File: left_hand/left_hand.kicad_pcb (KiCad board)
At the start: 2 copper layers, 75 x 85 mm, 48 parts, among them J1 8P8C_Shielded, J2 Conn_01x08, J3 Conn_01x03, J4 Conn_01x08, J5 Conn_02x02_Top_Bottom, J6 Screw_Terminal_01x10, M1 Motor_Servo, M2 Motor_Servo, M3 Motor_Servo, M4 Motor_Servo, M5 Motor_Servo, Q1 Q_NMOS_GDS, Q2 Q_NMOS_GDS, Q3 Q_NMOS_GDS, Q4 Q_NMOS_GDS, Q5 Q_NMOS_GDS, U1 MCP23017_SP, U2 PCA9615DP, U3 PCA9685PW

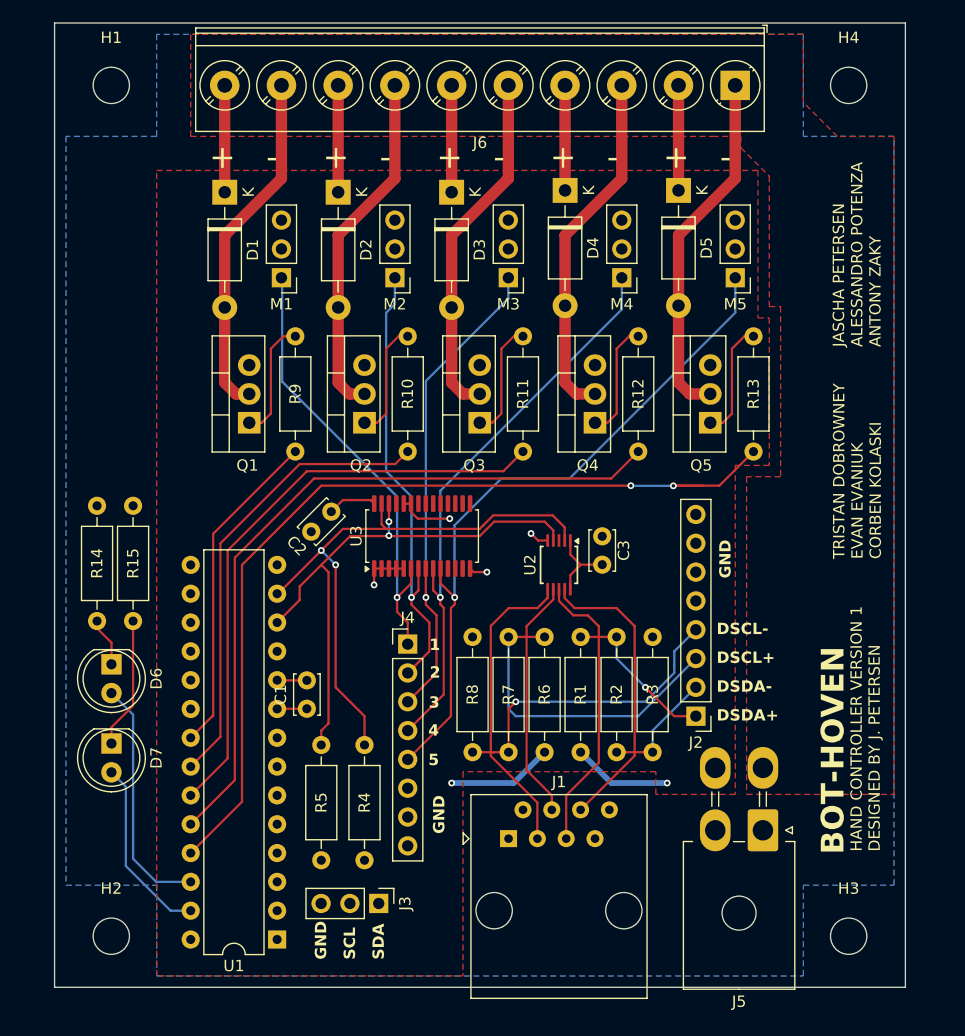
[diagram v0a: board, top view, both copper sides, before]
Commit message: Added current and voltage sensing on control board
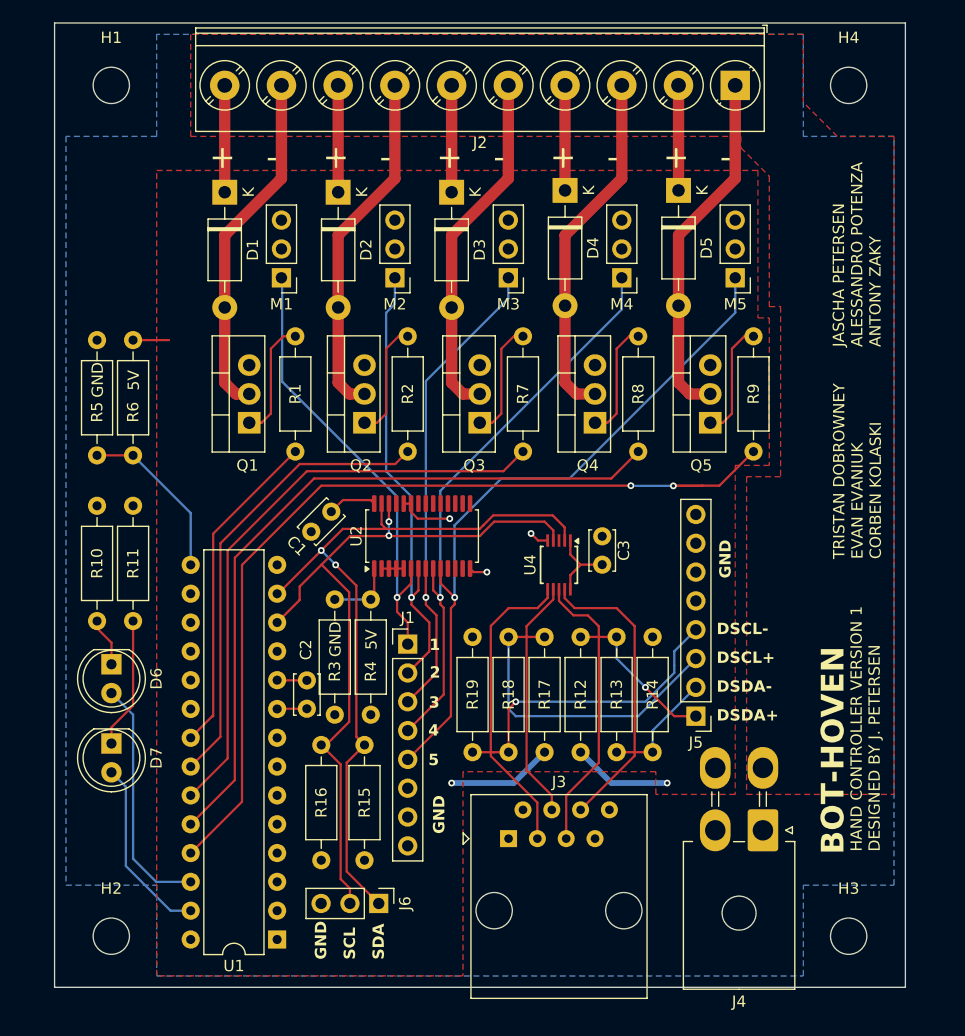
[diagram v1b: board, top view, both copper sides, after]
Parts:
- added R3: 0R, Resistor_THT:R_Axial_DIN0207_L6.3mm_D2.5mm_P10.16mm_Horizontal, F.Cu at (139.7, 107.3)
- added R4: 0R, Resistor_THT:R_Axial_DIN0207_L6.3mm_D2.5mm_P10.16mm_Horizontal, F.Cu at (142.9, 107.3)
- added R5: 0R, Resistor_THT:R_Axial_DIN0207_L6.3mm_D2.5mm_P10.16mm_Horizontal, F.Cu at (118.7, 94.6)
- added R6: 0R, Resistor_THT:R_Axial_DIN0207_L6.3mm_D2.5mm_P10.16mm_Horizontal, F.Cu at (121.9, 94.6)
- renumbered C2 to C1, C1 to C2, J4 to J1, J6 to J2, J1 to J3, J5 to J4, J2 to J5, J3 to J6, R9 to R1, R14 to R10, R15 to R11, R1 to R12, R2 to R13, R3 to R14, R4 to R15, R5 to R16, R6 to R17, R7 to R18, R8 to R19, R10 to R2, R11 to R7, R12 to R8, R13 to R9, U3 to U2, U2 to U4
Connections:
- U1 pad 15: GND -> Net-(U1-A0)
- U2 pad 1: GND -> Net-(U2-A0)
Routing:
- net SCL: track 49.2 -> 66.0 mm
- net SDA: track 51.0 -> 66.8 mm
- net Net-(U1-A0): track 0.00 -> 14.9 mm
- net Net-(U2-A0): track 0.00 -> 6.02 mm
- net +5V: track 31.7 -> 34.9 mm
- net GND: track 15.1 -> 13.0 mm, vias 4 -> 3
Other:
- board text added: "5V"

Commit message: Added limit switches to hand and readme
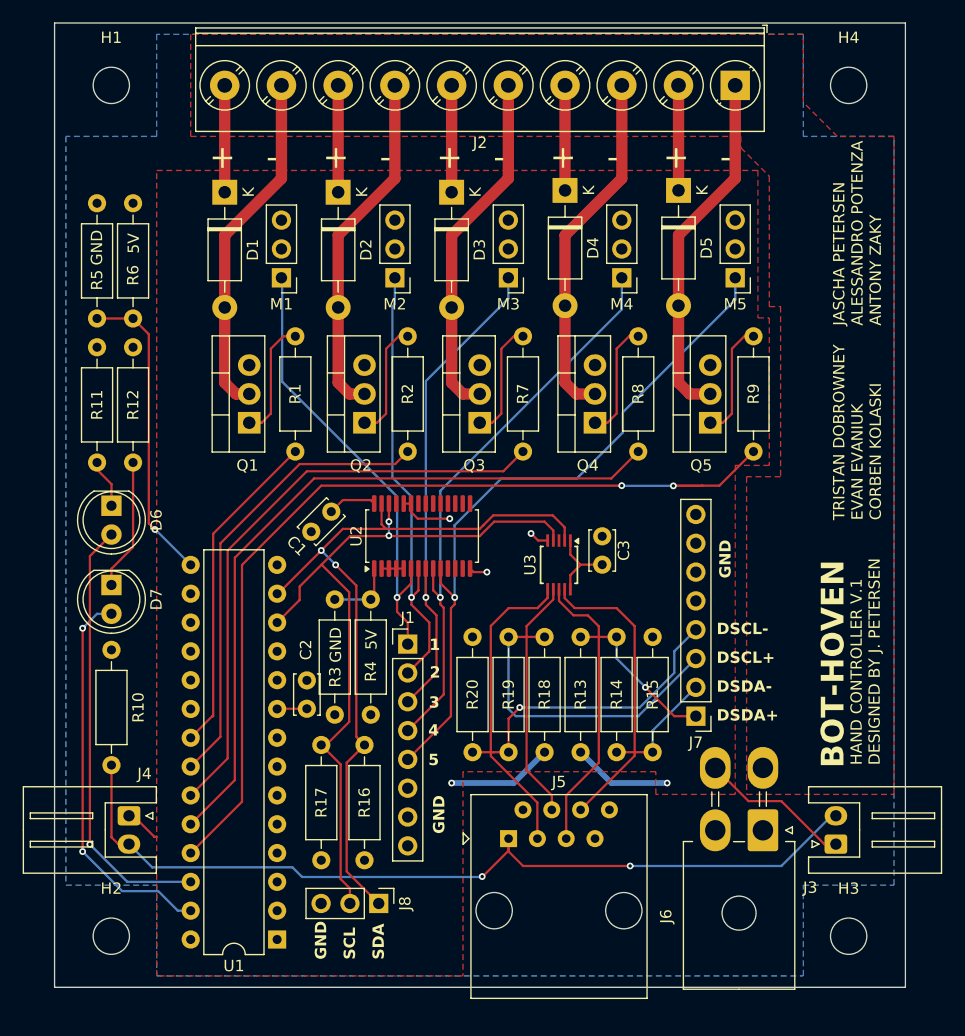
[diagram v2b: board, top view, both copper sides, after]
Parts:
- added J3: Conn_01x02, Connector_JST:JST_XH_S2B-XH-A_1x02_P2.50mm_Horizontal, F.Cu at (183.9, 128.9)
- added J4: Conn_01x02, Connector_JST:JST_XH_S2B-XH-A_1x02_P2.50mm_Horizontal, F.Cu at (121.6, 126.4)
- added R10: 10k, Resistor_THT:R_Axial_DIN0207_L6.3mm_D2.5mm_P10.16mm_Horizontal, F.Cu at (120.0, 111.8)
- moved D6 14.0 mm to (120.0, 99.1)
- moved D7 14.0 mm to (120.0, 106.0)
- moved R11 14.0 mm to (118.7, 95.2)
- moved R12 14.0 mm to (121.9, 95.2)
- moved R5 12.1 mm to (118.7, 82.5)
- moved R6 12.1 mm to (121.9, 82.5)
- renumbered J3 to J5, J4 to J6, J5 to J7, J6 to J8, R10 to R11, R11 to R12, R12 to R13, R13 to R14, R14 to R15, R15 to R16, R16 to R17, R17 to R18, R18 to R19, R19 to R20, U4 to U3
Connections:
- J5 pad 1: GND -> LIMIT_SW
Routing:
- net LIMIT_SW: track 0.00 -> 77.2 mm, vias 0 -> 2
- net LED2: track 16.1 -> 34.4 mm, vias 0 -> 2
- net LED1: track 21.3 -> 38.4 mm, vias 0 -> 1
- net +5V: track 34.9 -> 48.4 mm
- net Net-(U1-A0): track 14.9 -> 27.0 mm, vias 0 -> 1
- net GND: track 13.0 -> 10.4 mm
- net DSCL-: track 55.0 -> 54.5 mm
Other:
- board text added: "HAND CONTROLLER V.1"
- board text removed: "HAND CONTROLLER VERSION 1"

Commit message: Started layout of control board
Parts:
- added R21: 10k, Resistor_THT:R_Axial_DIN0207_L6.3mm_D2.5mm_P10.16mm_Horizontal, F.Cu at (180.3, 108.0)
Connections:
- J3 pad 2: LIMIT_SW -> LIMIT_SW_R
- J4 pad 2: LIMIT_SW -> LIMIT_SW_L
- J5 pad 1: LIMIT_SW -> LIMIT_SW_L
- J5 pad 8: GND -> LIMIT_SW_R
- R10 pad 2: LIMIT_SW -> LIMIT_SW_L
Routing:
- net LIMIT_SW: track 77.2 -> 0.00 mm, vias 2 -> 0
- net LIMIT_SW_L: track 0.00 -> 44.9 mm, vias 0 -> 1
- net LIMIT_SW_R: track 0.00 -> 34.2 mm, vias 0 -> 2

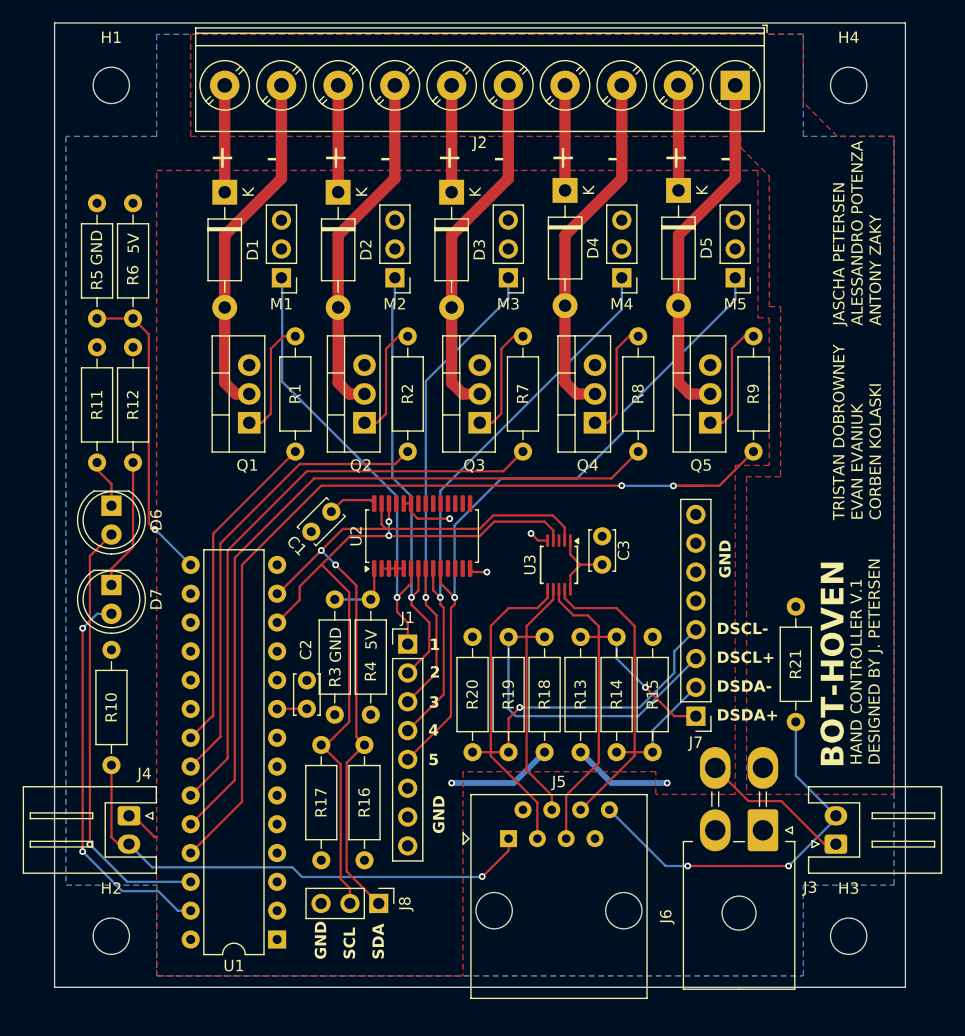
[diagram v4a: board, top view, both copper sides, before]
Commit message: Completed control board layout
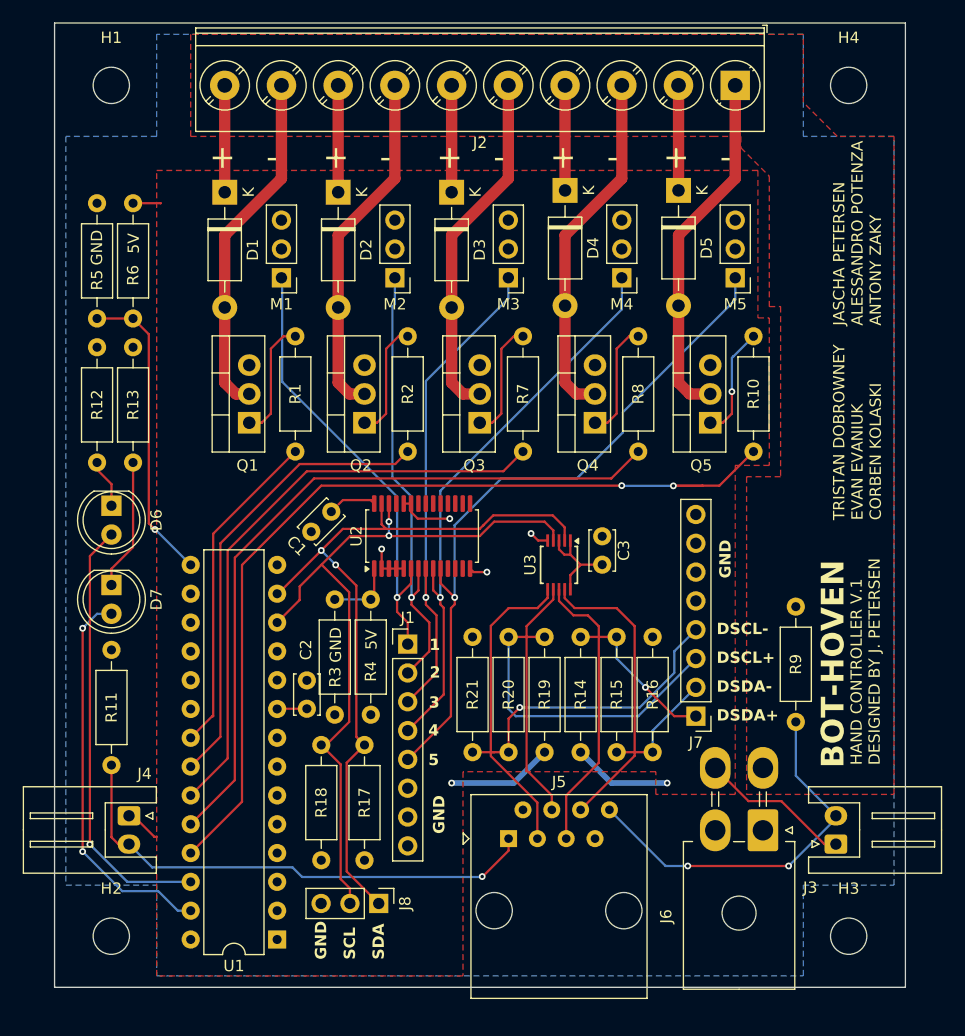
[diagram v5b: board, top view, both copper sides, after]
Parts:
- renumbered R9 to R10, R10 to R11, R11 to R12, R12 to R13, R13 to R14, R14 to R15, R15 to R16, R16 to R17, R17 to R18, R18 to R19, R19 to R20, R20 to R21, R21 to R9
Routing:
- net +5V: track 48.4 -> 52.8 mm
- net GND: track 10.4 -> 12.1 mm, vias 3 -> 4
- net Net-(Q5-G): track 10.3 -> 9.84 mm, vias 0 -> 1
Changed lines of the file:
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@@
 		(descr "Resistor, Axial_DIN0207 series, Axial, Horizontal, pin pitch=10.16mm, 0.25W = 1/4W, length*diameter=6.3*2.5mm^2, http://cdn-reichelt.de/documents/datenblatt/B400/1_4W%23YAG.pdf")
 		(tags "Resistor Axial_DIN0207 series Axial Horizontal pin pitch 10.16mm 0.25W = 1/4W length 6.3mm diameter 2.5mm")
-		(property "Reference" "R20"
+		(property "Reference" "R21"
 			(at 5.08 0 90)
 			(layer "F.SilkS")
@@
 		(descr "Resistor, Axial_DIN0207 series, Axial, Horizontal, pin pitch=10.16mm, 0.25W = 1/4W, length*diameter=6.3*2.5mm^2, http://cdn-reichelt.de/documents/datenblatt/B400/1_4W%23YAG.pdf")
 		(tags "Resistor Axial_DIN0207 series Axial Horizontal pin pitch 10.16mm 0.25W = 1/4W length 6.3mm diameter 2.5mm")
-		(property "Reference" "R15"
+		(property "Reference" "R16"
 			(at 5.08 0 90)
 			(layer "F.SilkS")
@@
 		(descr "Resistor, Axial_DIN0207 series, Axial, Horizontal, pin pitch=10.16mm, 0.25W = 1/4W, length*diameter=6.3*2.5mm^2, http://cdn-reichelt.de/documents/datenblatt/B400/1_4W%23YAG.pdf")
 		(tags "Resistor Axial_DIN0207 series Axial Horizontal pin pitch 10.16mm 0.25W = 1/4W length 6.3mm diameter 2.5mm")
-		(property "Reference" "R12"
+		(property "Reference" "R13"
 			(at 5.08 0 90)
 			(layer "F.SilkS")
@@
 		(descr "Resistor, Axial_DIN0207 series, Axial, Horizontal, pin pitch=10.16mm, 0.25W = 1/4W, length*diameter=6.3*2.5mm^2, http://cdn-reichelt.de/documents/datenblatt/B400/1_4W%23YAG.pdf")
 		(tags "Resistor Axial_DIN0207 series Axial Horizontal pin pitch 10.16mm 0.25W = 1/4W length 6.3mm diameter 2.5mm")
-		(property "Reference" "R11"
+		(property "Reference" "R12"
 			(at 5.08 0 90)
 			(layer "F.SilkS")
@@
 		(descr "Resistor, Axial_DIN0207 series, Axial, Horizontal, pin pitch=10.16mm, 0.25W = 1/4W, length*diameter=6.3*2.5mm^2, http://cdn-reichelt.de/documents/datenblatt/B400/1_4W%23YAG.pdf")
 		(tags "Resistor Axial_DIN0207 series Axial Horizontal pin pitch 10.16mm 0.25W = 1/4W length 6.3mm diameter 2.5mm")
-		(property "Reference" "R9"
+		(property "Reference" "R10"
 			(at 5.08 0 90)
 			(layer "F.SilkS")
@@
 		(descr "Resistor, Axial_DIN0207 series, Axial, Horizontal, pin pitch=10.16mm, 0.25W = 1/4W, length*diameter=6.3*2.5mm^2, http://cdn-reichelt.de/documents/datenblatt/B400/1_4W%23YAG.pdf")
 		(tags "Resistor Axial_DIN0207 series Axial Horizontal pin pitch 10.16mm 0.25W = 1/4W length 6.3mm diameter 2.5mm")
-		(property "Reference" "R17"
+		(property "Reference" "R18"
 			(at 5.08 0 90)
 			(layer "F.SilkS")
@@
 		(descr "Resistor, Axial_DIN0207 series, Axial, Horizontal, pin pitch=10.16mm, 0.25W = 1/4W, length*diameter=6.3*2.5mm^2, http://cdn-reichelt.de/documents/datenblatt/B400/1_4W%23YAG.pdf")
 		(tags "Resistor Axial_DIN0207 series Axial Horizontal pin pitch 10.16mm 0.25W = 1/4W length 6.3mm diameter 2.5mm")
-		(property "Reference" "R14"
+		(property "Reference" "R15"
 			(at 5.08 0 90)
 			(layer "F.SilkS")
@@
 		(descr "Resistor, Axial_DIN0207 series, Axial, Horizontal, pin pitch=10.16mm, 0.25W = 1/4W, length*diameter=6.3*2.5mm^2, http://cdn-reichelt.de/documents/datenblatt/B400/1_4W%23YAG.pdf")
 		(tags "Resistor Axial_DIN0207 series Axial Horizontal pin pitch 10.16mm 0.25W = 1/4W length 6.3mm diameter 2.5mm")
-		(property "Reference" "R10"
+		(property "Reference" "R11"
 			(at 5.08 0 90)
 			(layer "F.SilkS")
@@
 		(descr "Resistor, Axial_DIN0207 series, Axial, Horizontal, pin pitch=10.16mm, 0.25W = 1/4W, length*diameter=6.3*2.5mm^2, http://cdn-reichelt.de/documents/datenblatt/B400/1_4W%23YAG.pdf")
 		(tags "Resistor Axial_DIN0207 series Axial Horizontal pin pitch 10.16mm 0.25W = 1/4W length 6.3mm diameter 2.5mm")
-		(property "Reference" "R18"
+		(property "Reference" "R19"
 			(at 5.08 0 90)
 			(layer "F.SilkS")
@@
 		(descr "Resistor, Axial_DIN0207 series, Axial, Horizontal, pin pitch=10.16mm, 0.25W = 1/4W, length*diameter=6.3*2.5mm^2, http://cdn-reichelt.de/documents/datenblatt/B400/1_4W%23YAG.pdf")
 		(tags "Resistor Axial_DIN0207 series Axial Horizontal pin pitch 10.16mm 0.25W = 1/4W length 6.3mm diameter 2.5mm")
-		(property "Reference" "R19"
+		(property "Reference" "R20"
 			(at 5.08 0 90)
 			(layer "F.SilkS")
@@
 		(descr "Resistor, Axial_DIN0207 series, Axial, Horizontal, pin pitch=10.16mm, 0.25W = 1/4W, length*diameter=6.3*2.5mm^2, http://cdn-reichelt.de/documents/datenblatt/B400/1_4W%23YAG.pdf")
 		(tags "Resistor Axial_DIN0207 series Axial Horizontal pin pitch 10.16mm 0.25W = 1/4W length 6.3mm diameter 2.5mm")
-		(property "Reference" "R21"
+		(property "Reference" "R9"
 			(at 5.08 0 90)
 			(layer "F.SilkS")
@@
 		(descr "Resistor, Axial_DIN0207 series, Axial, Horizontal, pin pitch=10.16mm, 0.25W = 1/4W, length*diameter=6.3*2.5mm^2, http://cdn-reichelt.de/documents/datenblatt/B400/1_4W%23YAG.pdf")
 		(tags "Resistor Axial_DIN0207 series Axial Horizontal pin pitch 10.16mm 0.25W = 1/4W length 6.3mm diameter 2.5mm")
-		(property "Reference" "R13"
+		(property "Reference" "R14"
 			(at 5.08 0 90)
 			(layer "F.SilkS")
@@
 		(descr "Resistor, Axial_DIN0207 series, Axial, Horizontal, pin pitch=10.16mm, 0.25W = 1/4W, length*diameter=6.3*2.5mm^2, http://cdn-reichelt.de/documents/datenblatt/B400/1_4W%23YAG.pdf")
 		(tags "Resistor Axial_DIN0207 series Axial Horizontal pin pitch 10.16mm 0.25W = 1/4W length 6.3mm diameter 2.5mm")
-		(property "Reference" "R16"
+		(property "Reference" "R17"
 			(at 5.08 0 90)
 			(layer "F.SilkS")
@@
 	)
 	(segment
+		(start 124.355866 72.39)
+		(end 124.359377 72.386489)
+		(width 0.2)
+		(layer "F.Cu")
+		(net 1)
+	)
+	(segment
 		(start 163.91 104.25)
 		(end 161.35 104.25)
@@
 	)
 	(segment
+		(start 121.92 72.39)
+		(end 124.355866 72.39)
+		(width 0.2)
+		(layer "F.Cu")
+		(net 1)
+	)
+	(segment
 		(start 160.465 105.175)
 		(end 160.465 106.42)
@@
 	)
 	(segment
+		(start 159.465 102.12)
+		(end 159.465 102.895)
+		(width 0.2)
+		(layer "F.Cu")
+		(net 1)
+	)
+	(segment
 		(start 161.35 104.29)
 		(end 160.465 105.175)
@@
 	)
 	(segment
+		(start 159.935 103.365)
+		(end 160.465 103.365)
+		(width 0.2)
+		(layer "F.Cu")
+		(net 1)
+	)
+	(segment
 		(start 134.64 116.95)
 		(end 134.62 116.97)
@@
 	)
 	(segment
+		(start 159.465 102.895)
+		(end 159.935 103.365)
+		(width 0.2)
+		(layer "F.Cu")
+		(net 1)
+	)
+	(segment
 		(start 176.17 125.095)
 		(end 173.24 122.165)
@@
 	)
 	(segment
+		(start 143.833019 104.584481)
+		(end 143.825 104.5925)
+		(width 0.2)
+		(layer "F.Cu")
+		(net 2)
+	)
+	(segment
 		(start 157 101.5)
 		(end 157.62 102.12)
@@
 	)
 	(segment
+		(start 143.833019 102.867257)
+		(end 143.833019 104.584481)
+		(width 0.2)
+		(layer "F.Cu")
+		(net 2)
+	)
+	(segment
 		(start 157.62 102.12)
 		(end 158.465 102.12)
@@
 	)
 	(via
+		(at 143.833019 102.867257)
+		(size 0.6)
+		(drill 0.3)
+		(layers "F.Cu" "B.Cu")
+		(free yes)
+		(net 2)
+	)
+	(via
 		(at 149.836655 100.197653)
 		(size 0.6)
@@
 	)
 	(segment
-		(start 175.805 84.12)
-		(end 174.705 85.22)
+		(start 173.9 91.74)
+		(end 172.8 91.74)
+		(width 0.2)
+		(layer "F.Cu")
+		(net 24)
+	)
+	(segment
+		(start 174.705 89)
+		(end 174.705 90.935)
 		(width 0.2)
 		(layer "F.Cu")
@@
 		(net 24)
 	)
+	(via
+		(at 174.705 89)
+		(size 0.6)
+		(drill 0.3)
+		(layers "F.Cu" "B.Cu")
+		(net 24)
+	)
 	(segment
-		(start 174.705 85.22)
-		(end 174.705 90.935)
+		(start 174.705 89)
+		(end 174.705 86.023848)
 		(width 0.2)
-		(layer "F.Cu")
+		(layer "B.Cu")
 		(net 24)
 	)
 	(segment
-		(start 176.61 84.12)
-		(end 175.805 84.12)
+		(start 174.84468 85.884168)
+		(end 174.845832 85.884168)
 		(width 0.2)
-		(layer "F.Cu")
+		(layer "B.Cu")
 		(net 24)
 	)
 	(segment
-		(start 173.9 91.74)
-		(end 172.8 91.74)
+		(start 174.705 86.023848)
+		(end 174.84468 85.884168)
 		(width 0.2)
-		(layer "F.Cu")
+		(layer "B.Cu")
+		(net 24)
+	)
+	(segment
+		(start 174.845832 85.884168)
+		(end 176.61 84.12)
+		(width 0.2)
+		(layer "B.Cu")
 		(net 24)
 	)
